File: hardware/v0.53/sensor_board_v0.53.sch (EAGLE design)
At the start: 51 parts, among them J3 USB-MICROB, U1 ATMEGA328P, U3 OPA344, U4 RFM69HW, U5 FT231XS, U6 ADMP401, U7 SHT31-DIS, U8 MCP1703CB, U9 BMP280, Y1 16MHZ

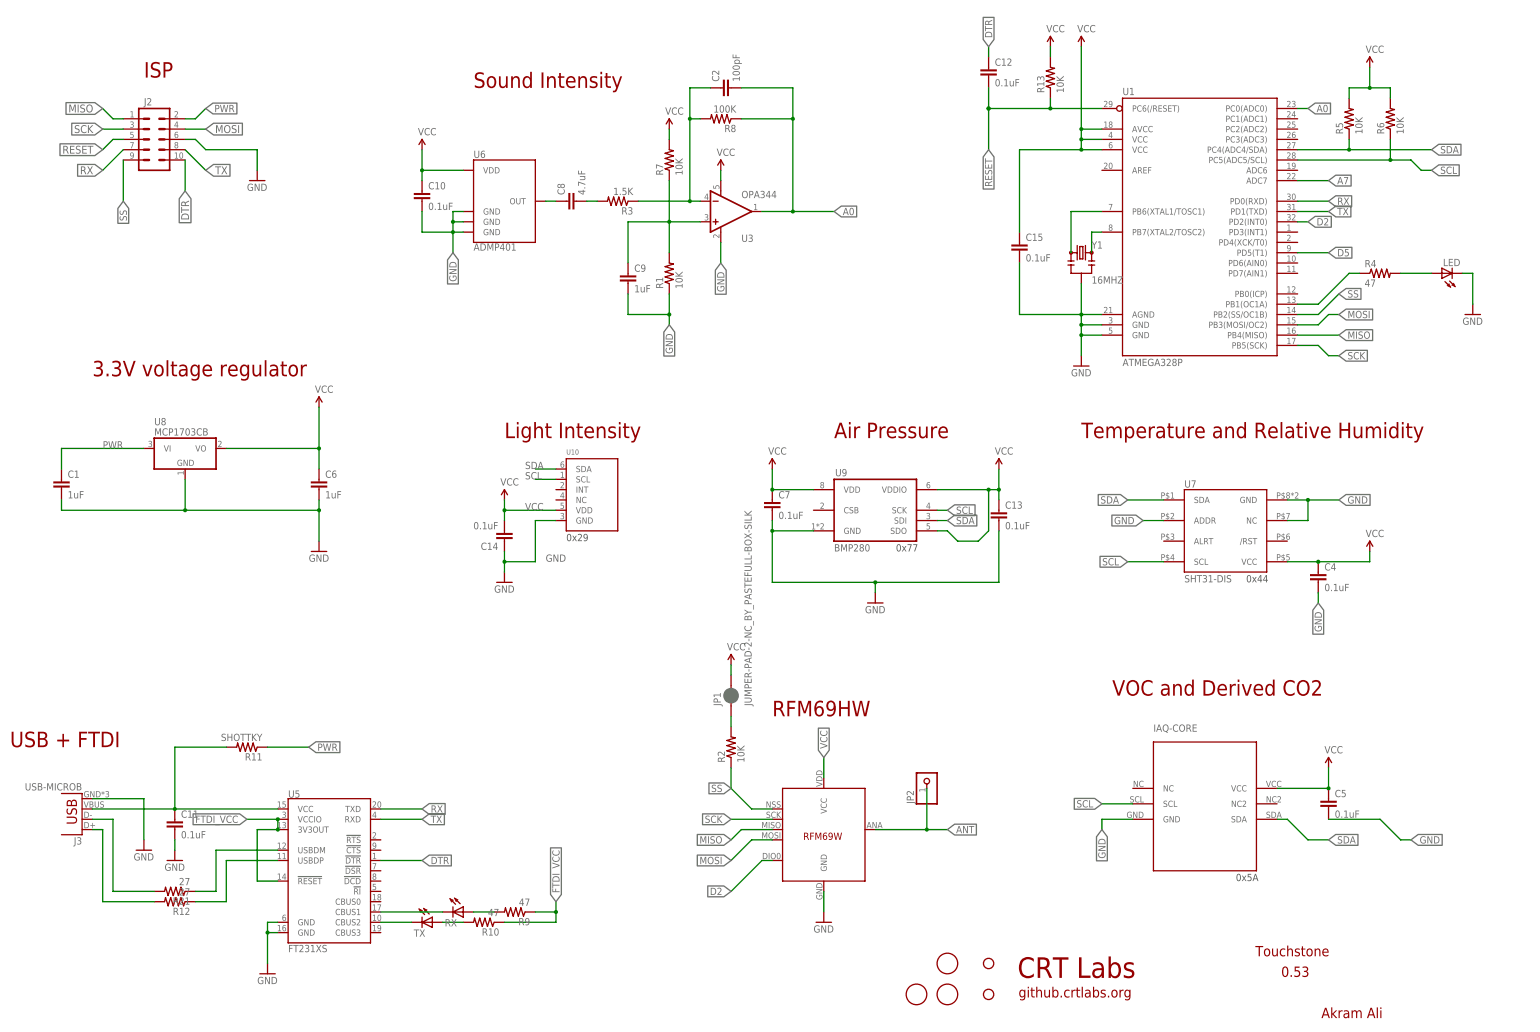
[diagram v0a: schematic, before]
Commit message: Update - Features added
- Replaced regular LED with RGB LED (NeoPixel from Adafruit)
- Adjusted overall dimensions to give slightly higher tolerance for mounting holes
- I2C pins broken out to headers
- Two digital pins broken out (for software serial)
- Extra power pins broken out (for powering external devices or connecting ground)
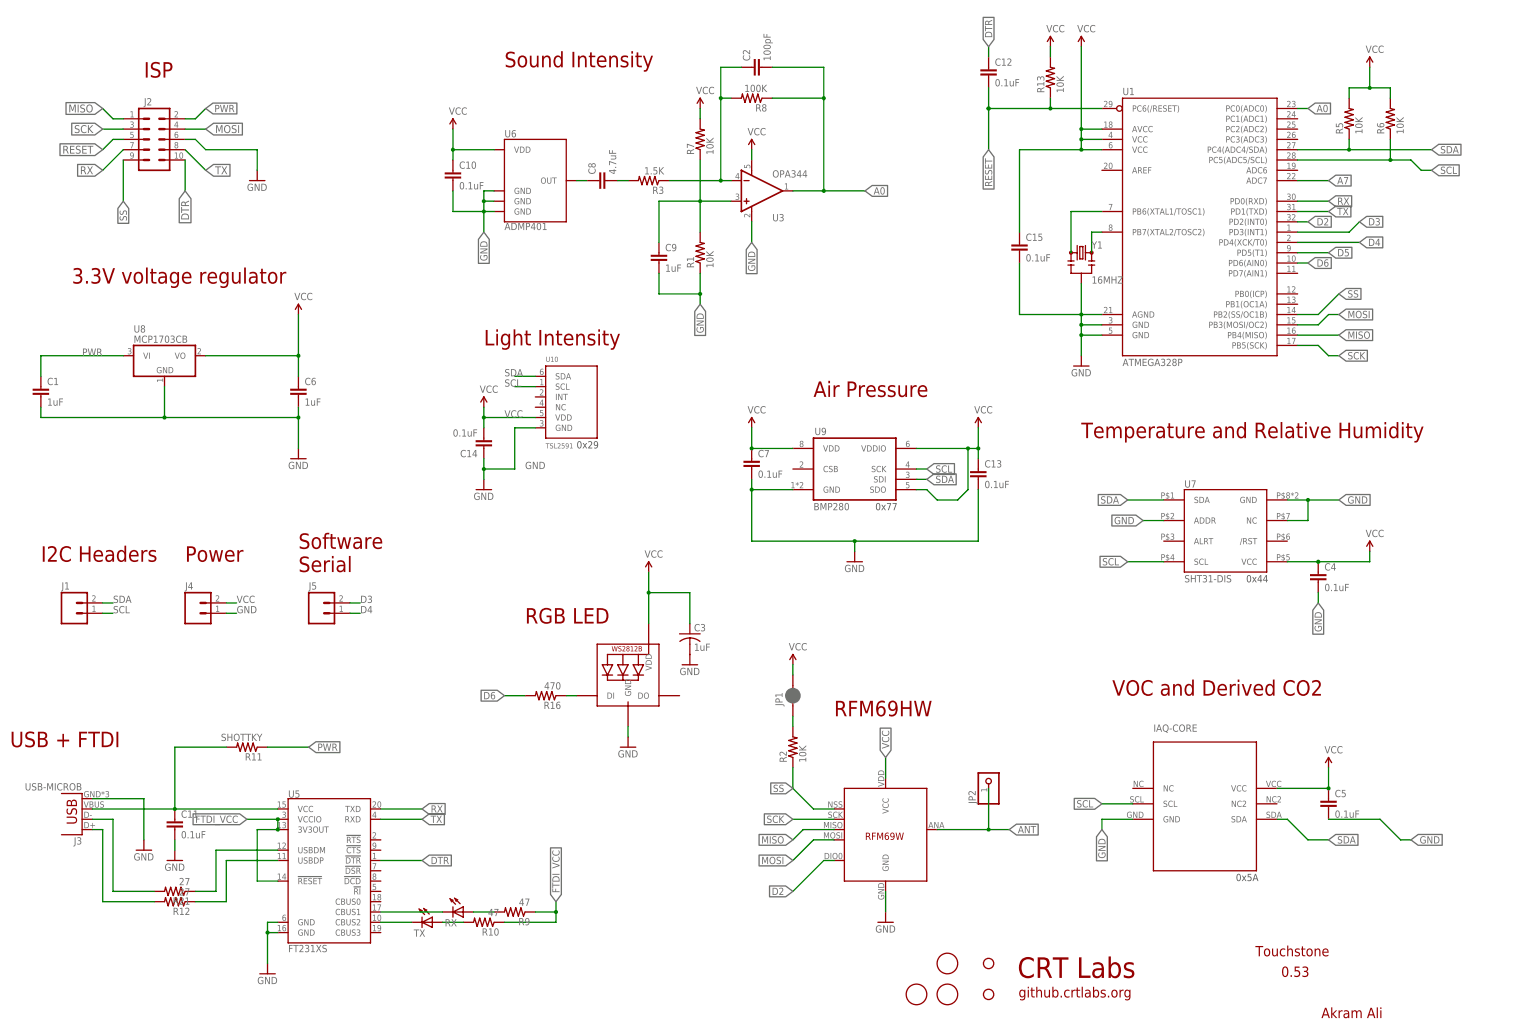
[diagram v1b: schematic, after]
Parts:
- removed LED: (no value), adafruit:LEDCHIPLED_0805
- removed R4: 47, SparkFun-Resistors:RESISTOR0805-RES
- added C3: 1uF, adafruit:C-USC0603K
- added J1, J4, J5: (no value), SparkFun-Connectors:M02PTH
- added LED1: WS2812B3535, adafruit:WS2812B3535
- added R16: 470, adafruit:R-US_R0603
- U10: value (none) -> TSL2591
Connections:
- removed net N$2: R4.1, U1.PB1(OC1A)
- removed net N$3: LED.A, R4.2
- new net D3: J5.2, U1.PD3(INT1)
- new net D4: J5.1, U1.PD4(XCK/T0)
- new net D6: R16.2, U1.PD6(AIN0)
- new net N$7: LED1.DI, R16.1
- net GND: now also C3.2, J4.1, LED1.GND; no longer LED.C
- net SCL: now also J1.1
- net SDA: now also J1.2
- net VCC: now also C3.1, J4.2, LED1.VDD
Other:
- note added: "I2C Headers"
- note added: "Power"
- note added: "RGB LED"
- note added: "Software Serial"
- moved on the sheet: C1, C10, C13, C14, C2, C6, C7, C8, C9, JP1, JP2, R1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

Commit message: Trace adjustments
Moved the radio and IAQ Core a bit to the left to allow more space for headers
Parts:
- R6: OC_NEWARK unknown -> (none)
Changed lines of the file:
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@@
 </part>
 <part name="R6" library="SparkFun-Resistors" deviceset="RESISTOR" device="0805-RES" value="10K">
-<attribute name="MF" value=""/>
-<attribute name="MPN" value=""/>
-<attribute name="OC_NEWARK" value="unknown"/>
+<attribute name="MPN" value=""/>
 </part>
 <part name="C4" library="SparkFun-Passives" deviceset="CAP" device="0805" value="0.1uF">
@@
 </instance>
 <instance part="R6" gate="G$1" x="284.48" y="109.22" rot="R90">
-<attribute name="OC_NEWARK" x="284.48" y="109.22" size="1.778" layer="96" rot="R270" display="off"/>
-<attribute name="MF" x="284.48" y="109.22" size="1.778" layer="96" rot="R270" display="off"/>
-<attribute name="MPN" x="284.48" y="109.22" size="1.778" layer="96" rot="R270" display="off"/>
+<attribute name="MPN" x="284.48" y="109.22" size="1.778" layer="96" rot="R90" display="off"/>
 </instance>
 <instance part="C4" gate="G$1" x="266.7" y="-5.08">

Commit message: BOM update - added MPNs
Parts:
- C1, C6, C9: MPN (none) -> CC0805ZRY5V8BB105; OC_NEWARK unknown -> (none)
- C10, C11, C14, C4, C5: MPN (none) -> CC0805KRX7R9BB104; OC_NEWARK unknown -> (none)
- C12, C13, C15, C7: MPN (none) -> CC0805KRX7R9BB104
- C2: MPN (none) -> CC0805JRNPOABN101; OC_NEWARK unknown -> (none)
- C3: MPN (none) -> CC0805ZRY5V8BB105
- C8: MPN (none) -> CC0805KKX7R6BB475; OC_NEWARK unknown -> (none)
- IAQ-CORE: MPN IAQ CORE -> IAQ-CORE C
- J3: MPN (none) -> 47346-0001
- LED1: MPN (none) -> SK6812 mini
- R1, R5, R7: MPN (none) -> RC0805FR-0710KL; OC_NEWARK unknown -> (none)
- R10, R9: MPN (none) -> RC0805FR-0747RL; OC_NEWARK unknown -> (none)
- R12, R21: MPN (none) -> RC0805FR-0727RL; OC_NEWARK unknown -> (none)
- R13, R2, R6: MPN (none) -> RC0805FR-0710KL
- R16: MPN (none) -> RC0805FR-07470RL
- R3: MPN (none) -> RC0805FR-071K5L; OC_NEWARK unknown -> (none)
- R8: MPN (none) -> RC0805FR-07100KL; OC_NEWARK unknown -> (none)
- U10: MPN (none) -> TSL25911FN
- U3: MPN (none) -> OPA344NA/3K
- U4: MPN (none) -> RFM69HW
- U5: MPN (none) -> FT231XQ-R
- U6: MPN (none) -> INMP401ACEZ-R7
- U9: MPN (none) -> BMP280

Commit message: BOM update
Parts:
- R11: MPN (none) -> SD0805S040S0R5
- RX, TX: MPN (none) -> LG R971-KN-1
- Y1: MPN (none) -> CSTCE16M0V53-R0
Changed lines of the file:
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@@
 <part name="Y1" library="SparkFun-FreqCtrl" deviceset="RESONATOR" device="16MHZ" value="16MHZ">
 <attribute name="MF" value=""/>
-<attribute name="MPN" value=""/>
+<attribute name="MPN" value="CSTCE16M0V53-R0"/>
 <attribute name="OC_NEWARK" value="unknown"/>
 </part>
@@
 <part name="RX" library="adafruit" deviceset="LED" device="CHIPLED_0805">
 <attribute name="MF" value=""/>
-<attribute name="MPN" value=""/>
+<attribute name="MPN" value="LG R971-KN-1"/>
 <attribute name="OC_NEWARK" value="unknown"/>
 </part>
 <part name="TX" library="adafruit" deviceset="LED" device="CHIPLED_0805">
 <attribute name="MF" value=""/>
-<attribute name="MPN" value=""/>
+<attribute name="MPN" value="LG R971-KN-1"/>
 <attribute name="OC_NEWARK" value="unknown"/>
 </part>
@@
 <part name="R11" library="SparkFun-Passives" deviceset="RESISTOR" device="0805-RES" value="SHOTTKY">
 <attribute name="MF" value=""/>
-<attribute name="MPN" value=""/>
+<attribute name="MPN" value="SD0805S040S0R5"/>
 <attribute name="OC_NEWARK" value="unknown"/>
 </part>
